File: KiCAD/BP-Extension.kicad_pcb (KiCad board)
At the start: 2 copper layers, 19.3 x 49.3 mm, 9 parts, among them P1 CONN_01X06, P2 CONN_01X01, SW1 SW_Push, U1 BP, U2 RFM69

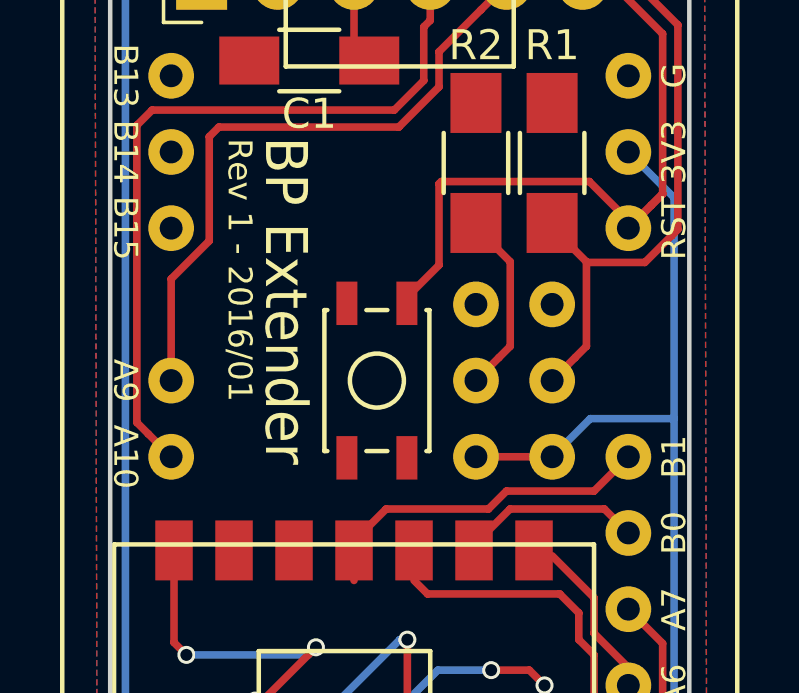
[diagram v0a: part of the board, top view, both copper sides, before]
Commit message: Moved 2x03 header to get rid of the offset, #8
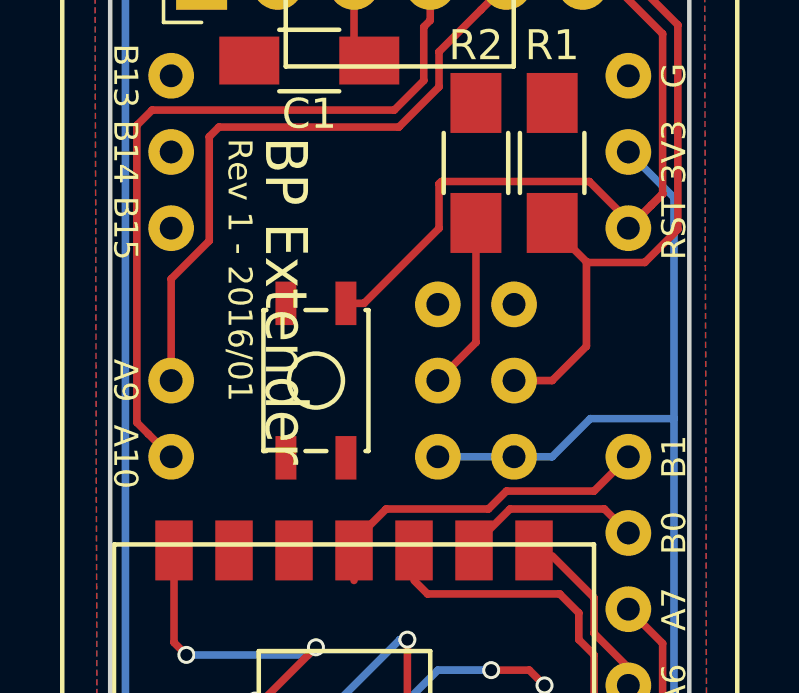
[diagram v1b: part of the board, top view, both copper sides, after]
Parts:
- moved SW1 2.03 mm to (146.1, 94.2)
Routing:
- net RTS: track 31.6 -> 32.8 mm
- net +3V3: track 64.1 -> 65.3 mm
- net DTR: track 23.5 -> 24.7 mm

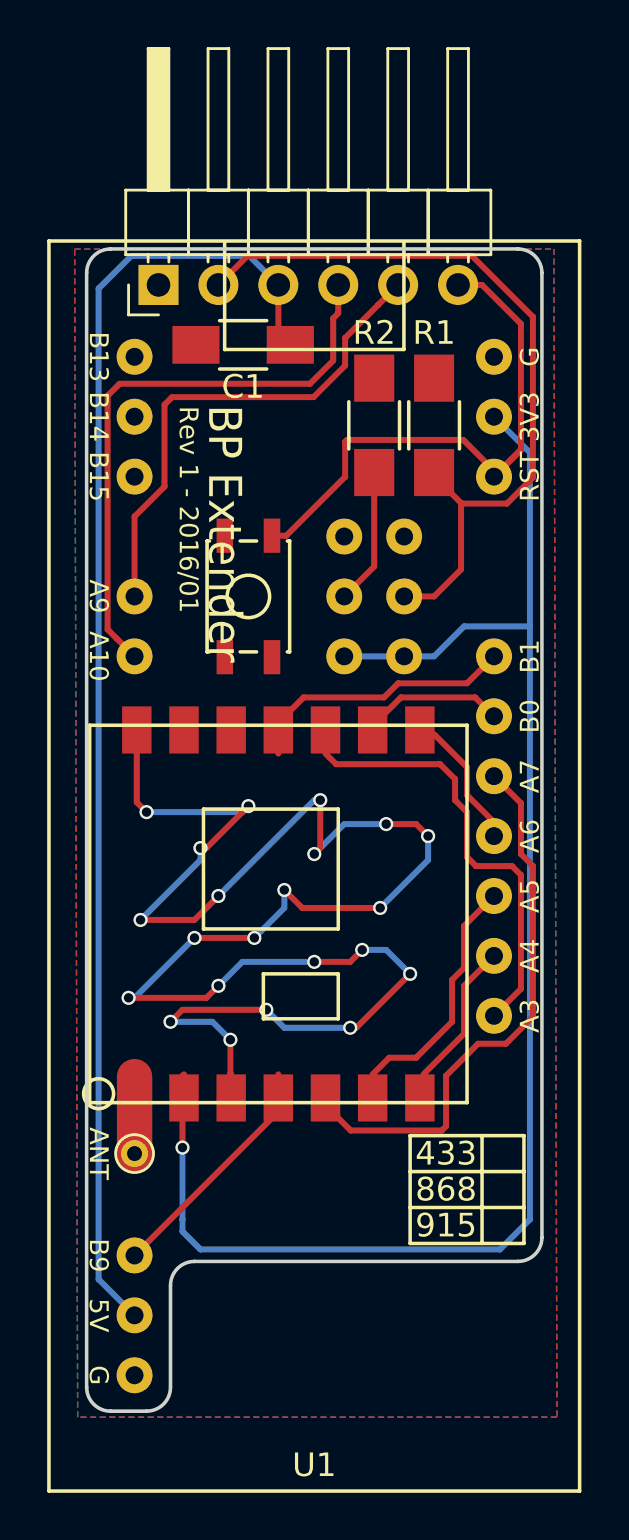
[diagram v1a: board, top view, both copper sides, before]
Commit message: Almost ready for rev2. fixes #9, fixes #8, fixes #1
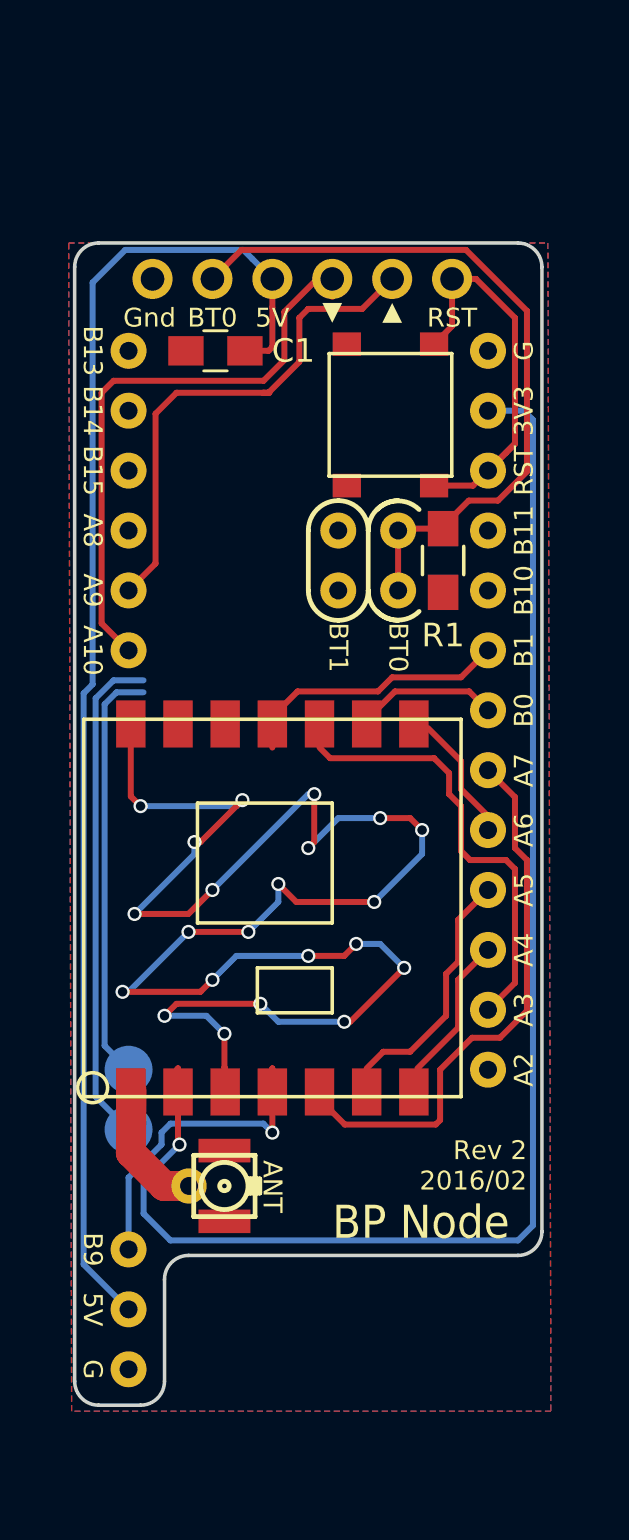
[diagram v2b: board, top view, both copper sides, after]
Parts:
- removed P2: CONN_01X01, Connect:PINTST
- removed R2: R, Resistors_SMD:R_1206_HandSoldering
- removed REF**: FREQ-LABEL, RFM69:FREQ-LABEL
- added AE1: Antenna_Shield, BP:U.FL-COAX, F.Cu at (145.0, 119.2)
- C1: footprint Capacitors_SMD:C_1206_HandSoldering -> Capacitors_SMD:C_0805_HandSoldering
- P1: footprint Pin_Headers:Pin_Header_Angled_1x06_Pitch2.54mm -> BP:Pin_Header_Angled_1x06_Pitch2.54mm
- R1: footprint Resistors_SMD:R_1206_HandSoldering -> Resistors_SMD:R_0805_HandSoldering
- SW1: footprint Buttons_Switches_SMD:SW_SPST_EVQP2 -> BP:SMD_BUTTON
- moved SW1 9.78 mm to (152.1, 86.5)
- moved R1 5.74 mm to (154.3, 92.7), turned to 90 degrees
- moved C1 1.20 mm to (144.7, 83.8)
- moved P1 0.36 mm to (142.0, 80.8)
- moved U1 0.36 mm to (148.6, 105.4)
- moved U2 0.36 mm to (147.1, 107.4)
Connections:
- U1 pad PB2: Net-(R2-Pad1) -> GND
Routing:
- net (no net): track 0.00 -> 39.0 mm
- net DTR: track 24.7 -> 17.8 mm
- net Net-(R2-Pad1): track 5.93 -> 0.00 mm
- net +3V3: track 65.3 -> 60.4 mm
- net DIO3: track 10.2 -> 14.9 mm, vias 0 -> 1
- net Net-(AE1-Pad1): track 3.40 -> 5.82 mm
- net RTS: track 32.8 -> 30.8 mm
- net Vin: track 55.6 -> 57.3 mm
- net RX: track 22.1 -> 22.9 mm
- net TX: track 25.8 -> 25.1 mm
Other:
- board size 19.3 x 49.3 mm -> 19.8 x 49.3 mm
- board text added: "A2"
- board text added: "A8"
- board text added: "B10"
- board text added: "B11"
- board text added: "BP Node"
- board text added: "BT0"
- board text added: "BT1"
- board text added: "Gnd"
- board text added: "Rev 2 2016/02"
- board text added: "▲"
- board text added: "▼"
- board text removed: "BP Extender"
- board text removed: "Rev 1 - 2016/01"

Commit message: Removed unnecessary files
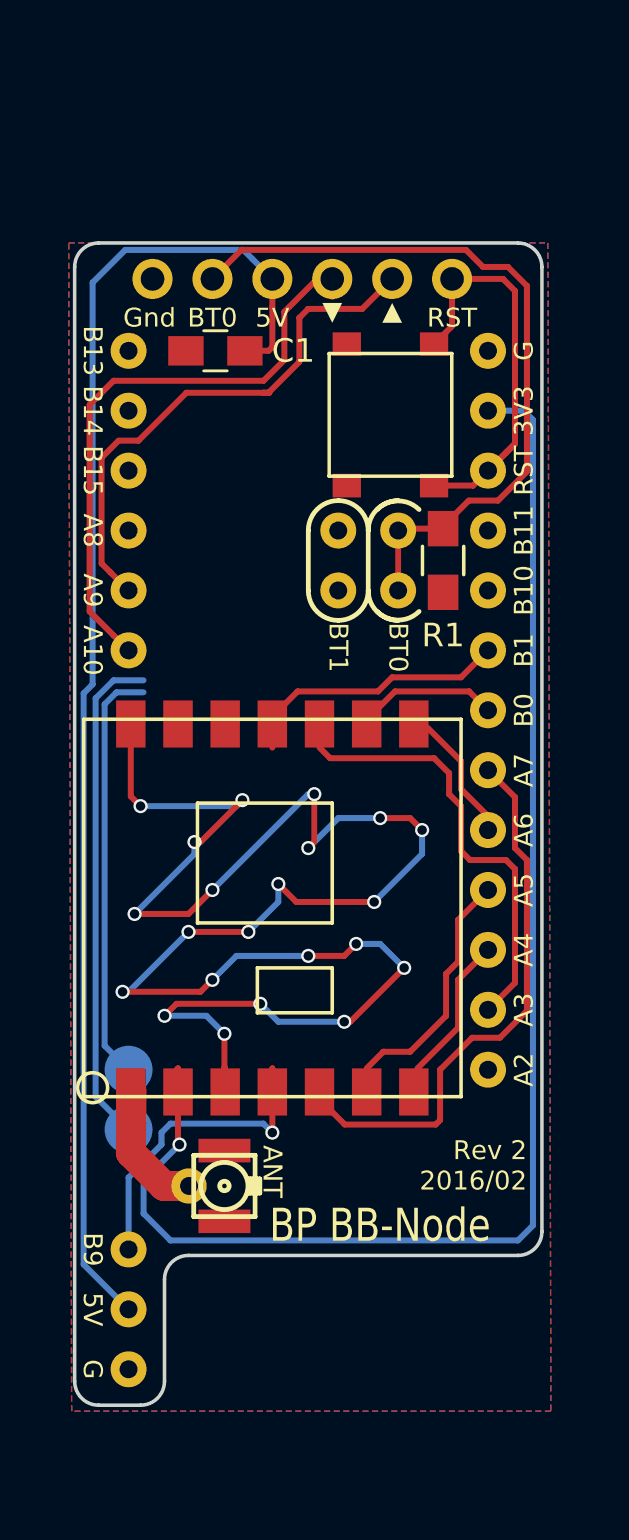
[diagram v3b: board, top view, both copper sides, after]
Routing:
- net RX: track 22.9 -> 24.1 mm
- net DTR: track 17.8 -> 18.5 mm
- net RTS: track 30.8 -> 31.4 mm
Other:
- board text added: "BP BB-Node"
- board text removed: "BP Node"
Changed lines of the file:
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@@
-(kicad_pcb (version 4) (host pcbnew 4.0.5)
+(kicad_pcb (version 4) (host pcbnew 4.0.4-stable)
   (general
     (links 32)
-    (no_connects 3)
+    (no_connects 2)
     (area 138.608999 79.172999 158.571001 128.599001)
     (thickness 1.6)
     (drawings 55)
-    (tracks 209)
+    (tracks 215)
     (zones 0)
     (modules 7)
@@
     (effects (font (size 0.8 0.8) (thickness 0.15)))
   )
-  (gr_text ANT (at 147.066 119.253 270) (layer F.SilkS)
+  (gr_text ANT (at 147.066 118.618 270) (layer F.SilkS)
     (effects (font (size 0.8 0.8) (thickness 0.15)))
   )
@@
     (effects (font (size 0.8 0.8) (thickness 0.15)) (justify right))
   )
-  (gr_text "BP Node" (at 149.606 120.777) (layer F.SilkS)
-    (effects (font (size 1.4 1.3) (thickness 0.3)) (justify left))
+  (gr_text "BP BB-Node" (at 146.939 120.904) (layer F.SilkS)
+    (effects (font (size 1.4 1.15) (thickness 0.2875)) (justify left))
   )
   (gr_arc (start 143.51 123.19) (end 142.494 123.19) (angle 90) (layer Edge.Cuts) (width 0.15))
@@
   (segment (start 141.066 102.712) (end 141.478 103.124) (width 0.254) (layer F.Cu) (net 1))
   (via (at 141.478 103.124) (size 0.6) (drill 0.4) (layers F.Cu B.Cu) (net 1))
+  (segment (start 144.526 80.772) (end 145.757001 79.540999) (width 0.254) (layer F.Cu) (net 2))
+  (segment (start 145.757001 79.540999) (end 155.276881 79.540999) (width 0.254) (layer F.Cu) (net 2))
+  (segment (start 154.305 91.26) (end 154.305 91.36) (width 0.254) (layer F.Cu) (net 2))
+  (segment (start 155.276881 79.540999) (end 155.999872 80.26399) (width 0.254) (layer F.Cu) (net 2))
+  (segment (start 155.999872 80.26399) (end 157.055425 80.26399) (width 0.254) (layer F.Cu) (net 2))
+  (segment (start 157.055425 80.26399) (end 157.861011 81.069576) (width 0.254) (layer F.Cu) (net 2))
+  (segment (start 157.861011 81.069576) (end 157.861011 88.940631) (width 0.254) (layer F.Cu) (net 2))
+  (segment (start 155.395 90.17) (end 154.305 91.26) (width 0.254) (layer F.Cu) (net 2))
+  (segment (start 157.861011 88.940631) (end 156.631642 90.17) (width 0.254) (layer F.Cu) (net 2))
+  (segment (start 156.631642 90.17) (end 155.395 90.17) (width 0.254) (layer F.Cu) (net 2))
   (segment (start 154.305 91.36) (end 152.48 91.36) (width 0.254) (layer F.Cu) (net 2))
   (segment (start 152.48 91.36) (end 152.4 91.44) (width 0.254) (layer F.Cu) (net 2))
-  (segment (start 157.861011 82.125129) (end 157.861011 88.773) (width 0.254) (layer F.Cu) (net 2))
-  (segment (start 155.395 90.17) (end 156.631642 90.17) (width 0.254) (layer F.Cu) (net 2))
-  (segment (start 156.631642 90.17) (end 157.861011 88.940631) (width 0.254) (layer F.Cu) (net 2))
-  (segment (start 157.861011 88.940631) (end 157.861011 88.773) (width 0.254) (layer F.Cu) (net 2))
-  (segment (start 154.305 91.36) (end 154.305 91.26) (width 0.254) (layer F.Cu) (net 2))
-  (segment (start 154.305 91.26) (end 155.395 90.17) (width 0.254) (layer F.Cu) (net 2))
-  (segment (start 144.526 80.772) (end 145.757001 79.540999) (width 0.254) (layer F.Cu) (net 2))
-  (segment (start 145.757001 79.540999) (end 155.276881 79.540999) (width 0.254) (layer F.Cu) (net 2))
-  (segment (start 155.276881 79.540999) (end 157.861011 82.125129) (width 0.254) (layer F.Cu) (net 2))
   (segment (start 152.4 93.98) (end 152.4 91.44) (width 0.254) (layer F.Cu) (net 2))
+  (segment (start 157.353001 81.28) (end 157.353001 82.423001) (width 0.254) (layer F.Cu) (net 3))
+  (segment (start 154.686 80.772) (end 156.845001 80.772) (width 0.254) (layer F.Cu) (net 3))
+  (segment (start 156.845001 80.772) (end 157.353001 81.28) (width 0.254) (layer F.Cu) (net 3))
   (segment (start 153.924 89.535) (end 155.575 89.535) (width 0.254) (layer F.Cu) (net 3))
   (segment (start 155.575 89.535) (end 156.21 88.9) (width 0.254) (layer F.Cu) (net 3))
@@
   (segment (start 156.21 88.9) (end 156.21 88.646) (width 0.254) (layer F.Cu) (net 3))
   (segment (start 157.353001 87.756999) (end 157.353001 82.423001) (width 0.254) (layer F.Cu) (net 3))
-  (segment (start 157.353001 82.423001) (end 155.702 80.772) (width 0.254) (layer F.Cu) (net 3))
-  (segment (start 155.702 80.772) (end 154.686 80.772) (width 0.254) (layer F.Cu) (net 3))
   (segment (start 156.21 88.9) (end 157.353001 87.756999) (width 0.254) (layer F.Cu) (net 3))
   (segment (start 157.353001 87.756999) (end 156.971999 88.138001) (width 0.254) (layer F.Cu) (net 3))
@@
   (via (at 143.129 117.475) (size 0.6) (drill 0.4) (layers F.Cu B.Cu) (net 4))
   (segment (start 143.066 114.242) (end 143.002 114.306) (width 0.254) (layer F.Cu) (net 4))
-  (segment (start 140.97 96.52) (end 139.826999 95.376999) (width 0.254) (layer F.Cu) (net 5))
-  (segment (start 139.826999 95.376999) (end 139.826999 85.598001) (width 0.254) (layer F.Cu) (net 5))
-  (segment (start 139.826999 85.598001) (end 140.335 85.09) (width 0.254) (layer F.Cu) (net 5))
-  (segment (start 140.335 85.09) (end 146.693802 85.09) (width 0.254) (layer F.Cu) (net 5))
-  (segment (start 148.971 80.772) (end 149.606 80.772) (width 0.254) (layer F.Cu) (net 5))
-  (segment (start 146.693802 85.09) (end 147.574 84.209802) (width 0.254) (layer F.Cu) (net 5))
-  (segment (start 147.574 84.209802) (end 147.574 82.169) (width 0.254) (layer F.Cu) (net 5))
-  (segment (start 147.574 82.169) (end 148.971 80.772) (width 0.254) (layer F.Cu) (net 5))
+  (segment (start 149.606 80.772) (end 148.971 80.772) (width 0.254) (layer F.Cu) (net 5))
+  (segment (start 148.971 80.772) (end 147.574 82.169) (width 0.254) (layer F.Cu) (net 5))
+  (segment (start 139.318989 94.868989) (end 140.335 95.885) (width 0.254) (layer F.Cu) (net 5))
+  (segment (start 147.574 82.169) (end 147.574 84.209802) (width 0.254) (layer F.Cu) (net 5))
+  (segment (start 147.574 84.209802) (end 146.693802 85.09) (width 0.254) (layer F.Cu) (net 5))
+  (segment (start 146.693802 85.09) (end 140.335 85.09) (width 0.254) (layer F.Cu) (net 5))
+  (segment (start 140.335 85.09) (end 139.318989 86.106011) (width 0.254) (layer F.Cu) (net 5))
+  (segment (start 139.318989 86.106011) (end 139.318989 94.868989) (width 0.254) (layer F.Cu) (net 5))
+  (segment (start 140.335 95.885) (end 140.97 96.52) (width 0.254) (layer F.Cu) (net 5))
   (segment (start 149.606 80.772) (end 149.606 81.534) (width 0.254) (layer F.Cu) (net 5))
+  (segment (start 146.685 85.598011) (end 143.423631 85.598011) (width 0.254) (layer F.Cu) (net 6))
+  (segment (start 143.423631 85.598011) (end 141.391642 87.63) (width 0.254) (layer F.Cu) (net 6))
+  (segment (start 141.391642 87.63) (end 140.548358 87.63) (width 0.254) (layer F.Cu) (net 6))
+  (segment (start 139.826999 88.351359) (end 139.826999 92.836999) (width 0.254) (layer F.Cu) (net 6))
+  (segment (start 139.826999 92.836999) (end 140.208001 93.218001) (width 0.254) (layer F.Cu) (net 6))
+  (segment (start 140.548358 87.63) (end 139.826999 88.351359) (width 0.254) (layer F.Cu) (net 6))
+  (segment (start 140.208001 93.218001) (end 140.97 93.98) (width 0.254) (layer F.Cu) (net 6))
   (segment (start 151.638 80.772) (end 152.146 80.772) (width 0.254) (layer F.Cu) (net 6))
   (segment (start 146.685 85.598011) (end 146.939 85.598008) (width 0.254) (layer F.Cu) (net 6))
@@
   (segment (start 148.59 82.042) (end 148.59001 82.04201) (width 0.254) (layer F.Cu) (net 6))
   (segment (start 148.59001 82.04201) (end 150.87599 82.04201) (width 0.254) (layer F.Cu) (net 6))
-  (segment (start 140.97 93.98) (end 142.113001 92.836999) (width 0.254) (layer F.Cu) (net 6))
-  (segment (start 142.113001 92.836999) (end 142.113001 86.486999) (width 0.254) (layer F.Cu) (net 6))
-  (segment (start 143.001989 85.598011) (end 146.685 85.598011) (width 0.254) (layer F.Cu) (net 6))
-  (segment (start 142.113001 86.486999) (end 143.001989 85.598011) (width 0.254) (layer F.Cu) (net 6))
   (segment (start 146.685 85.598011) (end 146.811989 85.598011) (width 0.254) (layer F.Cu) (net 6))
   (segment (start 152.146 80.772) (end 152.146 81.174198) (width 0.254) (layer F.Cu) (net 6))
@@
   (segment (start 146.685 116.586) (end 147.066 116.967) (width 0.254) (layer B.Cu) (net 15))
   (via (at 147.066 116.967) (size 0.6) (drill 0.4) (layers F.Cu B.Cu) (net 15))
-  (segment (start 147.066 114.242) (end 147.066 116.967) (width 0.254) (layer F.Cu) (net 15) (status 400000))
+  (segment (start 147.066 114.242) (end 147.066 116.967) (width 0.254) (layer F.Cu) (net 15))
   (segment (start 147.066 115.824) (end 147.066 114.242) (width 0.254) (layer F.Cu) (net 15))
   (segment (start 143.534 119.229) (end 142.47334 119.229) (width 1.27) (layer F.Cu) (net 16))

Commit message: On the way to rev2
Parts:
- added R2: R, Resistors_SMD:R_0805_HandSoldering, F.Cu at (146.1, 94.6)
- added R3: R, Resistors_SMD:R_0805_HandSoldering, F.Cu at (146.1, 96.5)
- added U3: M24M02-DR, Housings_SOIC:SOIC-8_3.9x4.9mm_Pitch1.27mm, F.Cu at (145.4, 89.5)
- moved AE1 0.15 mm to (145.0, 119.4)
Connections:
- U1 pad PB6: (no net) -> SCL
- U1 pad PB7: (no net) -> SDA
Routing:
- net (no net): track 39.0 -> 0.00 mm
- net SDA: track 0.00 -> 28.6 mm, vias 0 -> 1
- net SCL: track 0.00 -> 26.5 mm, vias 0 -> 1
- net +3V3: track 60.4 -> 74.3 mm, vias 1 -> 2
- net DIO3: track 14.9 -> 13.7 mm
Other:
- net class Ant added: clearance 0.254, trace_width 1.27, via_dia 0.6, via_drill 0.4
- net class Power added: clearance 0.254, trace_width 0.3556, via_dia 0.6, via_drill 0.4
- board text added: "A0"
- board text added: "A1"
- board text added: "B8"
- board text added: "BPnode BB"
- board text added: "Rev 2 2017/02"
- board text removed: "BP BB-Node"
- board text removed: "Rev 2 2016/02"
